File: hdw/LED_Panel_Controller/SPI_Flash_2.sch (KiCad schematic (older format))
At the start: 14 parts, among them U2601 74LVC1G97, U2602 SST25VF080B-50-4I-S2AF

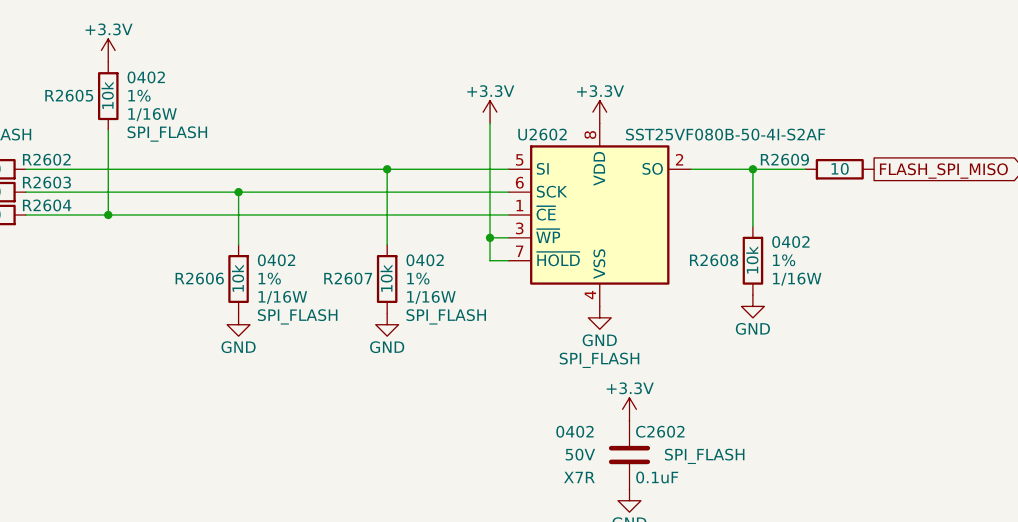
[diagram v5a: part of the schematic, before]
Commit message: fixed SPI flash pull resistors, more PCB placement
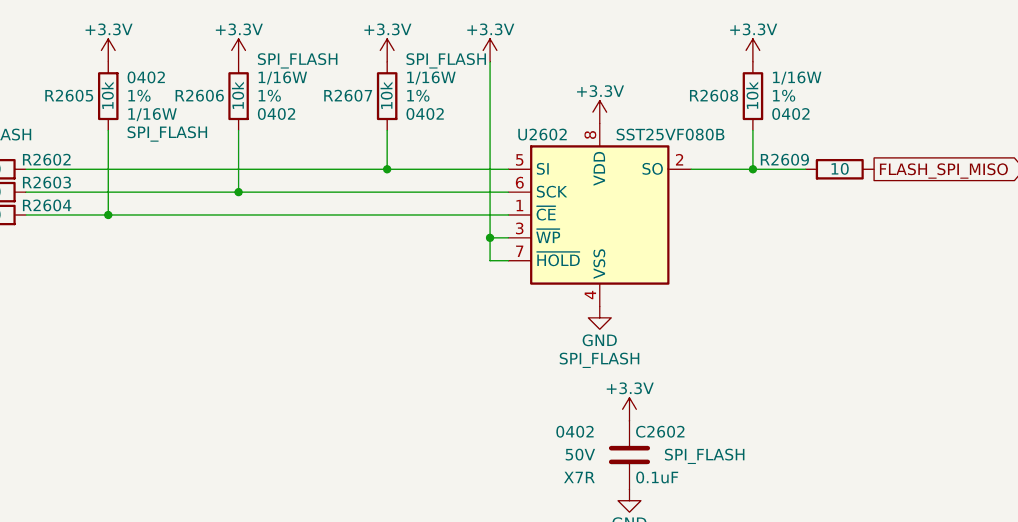
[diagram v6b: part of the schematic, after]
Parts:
- U2602: value SST25VF080B-50-4I-S2AF -> SST25VF080B
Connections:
- net +3V3: now also R2606.2, R2607.2, R2608.2
- net GND: no longer R2606.2, R2607.2, R2608.2
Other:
- moved on the sheet: R2606, R2607, R2608
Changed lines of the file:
@@
 L Custom_Library:R_Custom R2608
 U 1 1 6078626A
-P 6750 3850
-F 0 "R2608" H 6690 3850 50  0000 R CNN
-F 1 "10k" V 6750 3850 50  0000 C CNN
-F 2 "Resistors_SMD:R_0402" H 6750 3850 50  0001 C CNN
-F 3 "" H 6750 3850 50  0001 C CNN
-F 4 "0402" H 6830 3930 50  0000 L CNN "display_footprint"
-F 5 "1%" H 6830 3850 50  0000 L CNN "Tolerance"
-F 6 "1/16W" H 6830 3770 50  0000 L CNN "Wattage"
-F 7 "RMCF0402FT10K0CT-ND" H 7050 4250 60  0001 C CNN "Digi-Key PN"
-	1    6750 3850
-	1    0    0    -1
-$EndComp
-$Comp
-L power:GND #PWR02608
-U 1 1 6078626C
-P 5150 4080
-F 0 "#PWR02608" H 5150 3830 50  0001 C CNN
-F 1 "GND" H 5150 3930 50  0000 C CNN
-F 2 "" H 5150 4080 50  0001 C CNN
-F 3 "" H 5150 4080 50  0001 C CNN
-	1    5150 4080
-	1    0    0    -1
-$EndComp
-$Comp
-L power:GND #PWR02614
-U 1 1 5BB4EE7C
-P 6750 4000
-F 0 "#PWR02614" H 6750 3750 50  0001 C CNN
-F 1 "GND" H 6750 3850 50  0000 C CNN
-F 2 "" H 6750 4000 50  0001 C CNN
-F 3 "" H 6750 4000 50  0001 C CNN
-	1    6750 4000
-	1    0    0    -1
+P 6750 3130
+F 0 "R2608" H 6690 3130 50  0000 R CNN
+F 1 "10k" V 6750 3130 50  0000 C CNN
+F 2 "Resistors_SMD:R_0402" H 6750 3130 50  0001 C CNN
+F 3 "" H 6750 3130 50  0001 C CNN
+F 4 "0402" H 6830 3210 50  0000 L CNN "display_footprint"
+F 5 "1%" H 6830 3130 50  0000 L CNN "Tolerance"
+F 6 "1/16W" H 6830 3050 50  0000 L CNN "Wattage"
+F 7 "RMCF0402FT10K0CT-ND" H 7050 3530 60  0001 C CNN "Digi-Key PN"
+	1    6750 3130
+	1    0    0    1
 $EndComp
 $Comp
@@
 $EndComp
 Wire Wire Line
-	5150 3450 5150 3780
-Connection ~ 5150 3450
-Wire Wire Line
-	5150 3450 5680 3450
-Wire Wire Line
 	3930 3280 3930 3650
 Wire Wire Line
 	3930 3650 5680 3650
 Connection ~ 3930 3650
-Wire Wire Line
-	6980 3450 6750 3450
-Wire Wire Line
-	6750 3700 6750 3450
-Connection ~ 6750 3450
-Wire Wire Line
-	6750 3450 6480 3450
 Text GLabel 7280 3450 2    50   Output ~ 0
 FLASH_SPI_MISO
@@
 P 6080 3650
 F 0 "U2602" H 5830 4000 50  0000 C CNN
-F 1 "SST25VF080B-50-4I-S2AF" H 6630 4000 50  0000 C CNN
+F 1 "SST25VF080B" H 6630 4000 50  0000 R CNN
 F 2 "Package_SO:SOIC-8_5.275x5.275mm_P1.27mm" H 6080 2950 50  0001 C CNN
 F 3 "http://ww1.microchip.com/downloads/en/DeviceDoc/20005045C.pdf" H 6030 4200 50  0001 C CNN
@@
 L power:+3.3V #PWR02609
 U 1 1 6078630C
-P 5600 3250
-F 0 "#PWR02609" H 5600 3100 50  0001 C CNN
-F 1 "+3.3V" H 5600 3390 50  0000 C CNN
-F 2 "" H 5600 3250 50  0001 C CNN
-F 3 "" H 5600 3250 50  0001 C CNN
-	1    5600 3250
+P 5600 2980
+F 0 "#PWR02609" H 5600 2830 50  0001 C CNN
+F 1 "+3.3V" H 5600 3120 50  0000 C CNN
+F 2 "" H 5600 2980 50  0001 C CNN
+F 3 "" H 5600 2980 50  0001 C CNN
+	1    5600 2980
 	1    0    0    -1
 $EndComp
@@
 	5680 3750 5600 3750
 Wire Wire Line
-	5600 3750 5600 3250
+	5600 3750 5600 2980
 Wire Wire Line
 	5680 3850 5600 3850
@@
 	5600 3850 5600 3750
 Connection ~ 5600 3750
-Wire Wire Line
-	3570 3550 4500 3550
 $Comp
 L Custom_Library:R_Custom R2606
 U 1 1 5F697048
-P 4500 3930
-F 0 "R2606" H 4440 3930 50  0000 R CNN
-F 1 "10k" V 4500 3930 50  0000 C CNN
-F 2 "Resistors_SMD:R_0402" H 4500 3930 50  0001 C CNN
-F 3 "" H 4500 3930 50  0001 C CNN
-F 4 "0402" H 4580 4010 50  0000 L CNN "display_footprint"
-F 5 "1%" H 4580 3930 50  0000 L CNN "Tolerance"
-F 6 "1/16W" H 4580 3850 50  0000 L CNN "Wattage"
-F 7 "RMCF0402FT10K0CT-ND" H 4800 4330 60  0001 C CNN "Digi-Key PN"
-F 8 "SPI_FLASH" H 4580 3770 50  0000 L CNN "Configuration"
-	1    4500 3930
-	1    0    0    -1
-$EndComp
-$Comp
-L power:GND #PWR02607
-U 1 1 6078631F
-P 4500 4080
-F 0 "#PWR02607" H 4500 3830 50  0001 C CNN
-F 1 "GND" H 4500 3930 50  0000 C CNN
-F 2 "" H 4500 4080 50  0001 C CNN
-F 3 "" H 4500 4080 50  0001 C CNN
-	1    4500 4080
-	1    0    0    -1
-$EndComp
-Wire Wire Line
-	3570 3450 5150 3450
-Wire Wire Line
-	4500 3550 4500 3780
-Connection ~ 4500 3550
-Wire Wire Line
-	4500 3550 5680 3550
+P 4500 3130
+F 0 "R2606" H 4440 3130 50  0000 R CNN
+F 1 "10k" V 4500 3130 50  0000 C CNN
+F 2 "Resistors_SMD:R_0402" H 4500 3130 50  0001 C CNN
+F 3 "" H 4500 3130 50  0001 C CNN
+F 4 "0402" H 4580 3210 50  0000 L CNN "display_footprint"
+F 5 "1%" H 4580 3130 50  0000 L CNN "Tolerance"
+F 6 "1/16W" H 4580 3050 50  0000 L CNN "Wattage"
+F 7 "RMCF0402FT10K0CT-ND" H 4800 3530 60  0001 C CNN "Digi-Key PN"
+F 8 "SPI_FLASH" H 4580 2970 50  0000 L CNN "Configuration"
+	1    4500 3130
+	1    0    0    1
+$EndComp
 $Comp
 L Custom_Library:R_Custom R2603
@@
 L Custom_Library:R_Custom R2607
 U 1 1 6026393A
-P 5150 3930
-F 0 "R2607" H 5090 3930 50  0000 R CNN
-F 1 "10k" V 5150 3930 50  0000 C CNN
-F 2 "Resistors_SMD:R_0402" H 5150 3930 50  0001 C CNN
-F 3 "" H 5150 3930 50  0001 C CNN
-F 4 "0402" H 5230 4010 50  0000 L CNN "display_footprint"
-F 5 "1%" H 5230 3930 50  0000 L CNN "Tolerance"
-F 6 "1/16W" H 5230 3850 50  0000 L CNN "Wattage"
-F 7 "RMCF0402FT10K0CT-ND" H 5450 4330 60  0001 C CNN "Digi-Key PN"
-F 8 "SPI_FLASH" H 5230 3770 50  0000 L CNN "Configuration"
-	1    5150 3930
-	1    0    0    -1
+P 5150 3130
+F 0 "R2607" H 5090 3130 50  0000 R CNN
+F 1 "10k" V 5150 3130 50  0000 C CNN
+F 2 "Resistors_SMD:R_0402" H 5150 3130 50  0001 C CNN
+F 3 "" H 5150 3130 50  0001 C CNN
+F 4 "0402" H 5230 3210 50  0000 L CNN "display_footprint"
+F 5 "1%" H 5230 3130 50  0000 L CNN "Tolerance"
+F 6 "1/16W" H 5230 3050 50  0000 L CNN "Wattage"
+F 7 "RMCF0402FT10K0CT-ND" H 5450 3530 60  0001 C CNN "Digi-Key PN"
+F 8 "SPI_FLASH" H 5230 2970 50  0000 L CNN "Configuration"
+	1    5150 3130
+	1    0    0    1
 $EndComp
 $Comp
@@
 	1    0    0    -1
 $EndComp
+Wire Wire Line
+	3570 3450 5150 3450
+Wire Wire Line
+	3570 3550 4500 3550
+$Comp
+L power:+3.3V #PWR0109
+U 1 1 6067AD21
+P 5150 2980
+F 0 "#PWR0109" H 5150 2830 50  0001 C CNN
+F 1 "+3.3V" H 5150 3120 50  0000 C CNN
+F 2 "" H 5150 2980 50  0001 C CNN
+F 3 "" H 5150 2980 50  0001 C CNN
+	1    5150 2980
+	1    0    0    -1
+$EndComp
+$Comp
+L power:+3.3V #PWR0110
+U 1 1 6067AF67
+P 4500 2980
+F 0 "#PWR0110" H 4500 2830 50  0001 C CNN
+F 1 "+3.3V" H 4500 3120 50  0000 C CNN
+F 2 "" H 4500 2980 50  0001 C CNN
+F 3 "" H 4500 2980 50  0001 C CNN
+	1    4500 2980
+	1    0    0    -1
+$EndComp
+Wire Wire Line
+	4500 3280 4500 3550
+Connection ~ 4500 3550
+Wire Wire Line
+	4500 3550 5680 3550
+Wire Wire Line
+	5150 3280 5150 3450
+Connection ~ 5150 3450
+Wire Wire Line
+	5150 3450 5680 3450
+Wire Wire Line
+	6480 3450 6750 3450
+Wire Wire Line
+	6750 3280 6750 3450
+Connection ~ 6750 3450
+Wire Wire Line
+	6750 3450 6980 3450
+$Comp
+L power:+3.3V #PWR0111
+U 1 1 6067C4E3
+P 6750 2980
+F 0 "#PWR0111" H 6750 2830 50  0001 C CNN
+F 1 "+3.3V" H 6750 3120 50  0000 C CNN
+F 2 "" H 6750 2980 50  0001 C CNN
+F 3 "" H 6750 2980 50  0001 C CNN
+	1    6750 2980
+	1    0    0    -1
+$EndComp

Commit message: added BOMs, some consolidation
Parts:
- C2601, C2602: Digi-Key PN 490-10701-1-ND -> 490-10698-1-ND
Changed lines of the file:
@@
 F 5 "50V" H 1860 6900 50  0000 R CNN "Voltage"
 F 6 "X7R" H 1860 6800 50  0000 R CNN "Dielectric"
-F 7 "490-10701-1-ND" H 2435 7400 60  0001 C CNN "Digi-Key PN"
+F 7 "490-10698-1-ND" H 2435 7400 60  0001 C CNN "Digi-Key PN"
 F 8 "SPI_FLASH" H 2340 6900 50  0000 C CNN "Configuration"
 	1    2010 6900
@@
 F 5 "50V" H 6060 4700 50  0000 R CNN "Voltage"
 F 6 "X7R" H 6060 4600 50  0000 R CNN "Dielectric"
-F 7 "490-10701-1-ND" H 6635 5200 60  0001 C CNN "Digi-Key PN"
+F 7 "490-10698-1-ND" H 6635 5200 60  0001 C CNN "Digi-Key PN"
 F 8 "SPI_FLASH" H 6540 4700 50  0000 C CNN "Configuration"
 	1    6210 4700
